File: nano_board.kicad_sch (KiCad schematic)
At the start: 23 parts, among them J1 RJ45

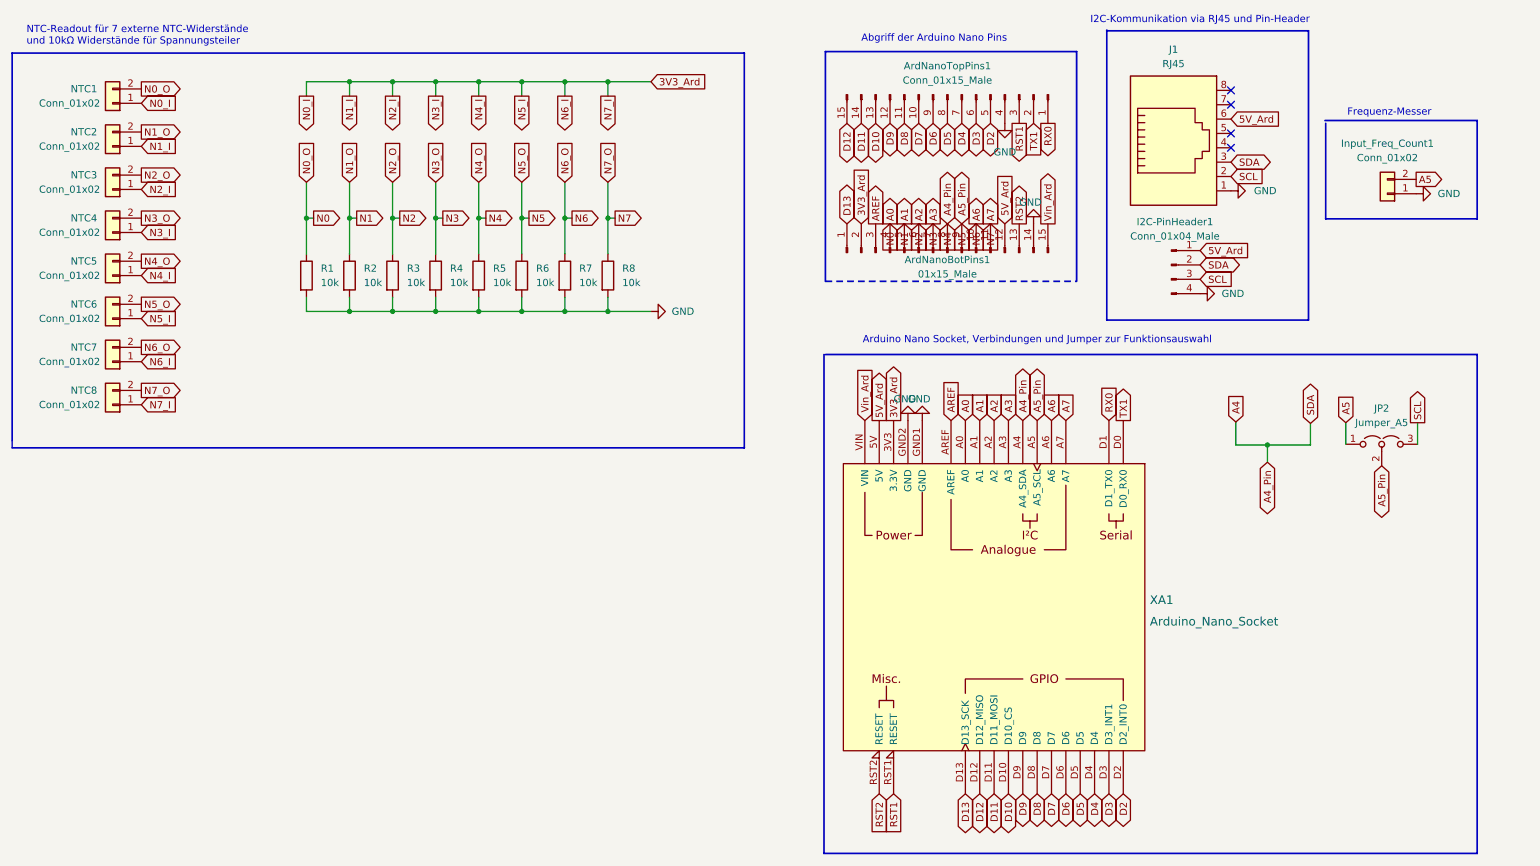
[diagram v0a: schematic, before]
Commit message: ADD: schematic as pdf
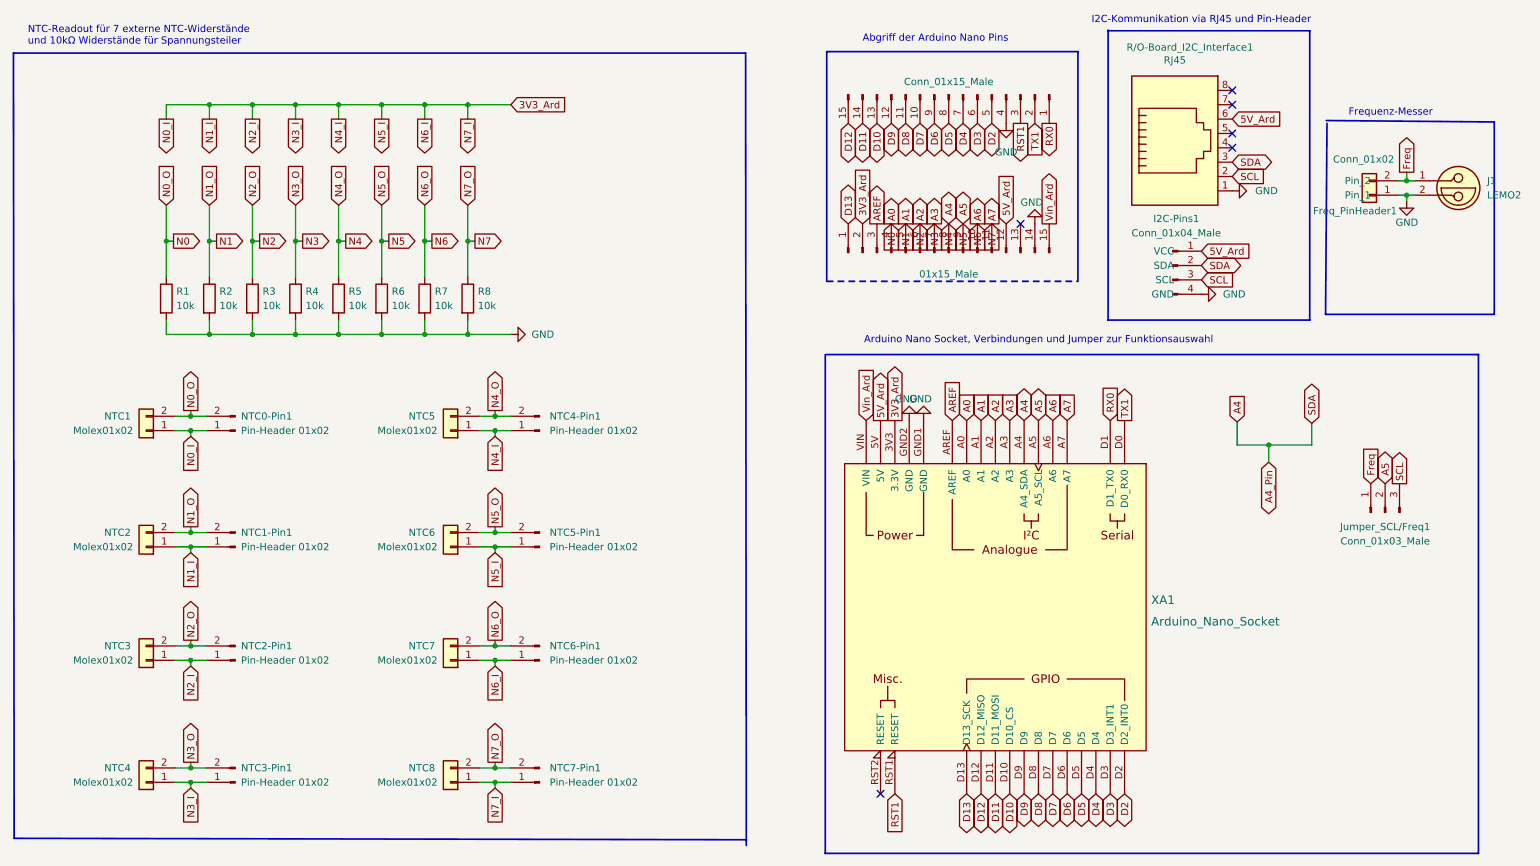
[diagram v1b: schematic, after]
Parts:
- removed JP2: Jumper_A5, Jumper:SolderJumper-3_P1.3mm_Open_Pad1.0x1.5mm_NumberLabels, symbol Jumper:Jumper_3_Open
- added J1: LEMO2, OwnFootprints:EPL.00.250.NTN, symbol Connector:LEMO2
- added Jumper_SCL/Freq1: Conn_01x03_Male, Connector_PinHeader_2.54mm:PinHeader_1x03_P2.54mm_Vertical, symbol Connector:Conn_01x03_Male
- added NTC0-Pin1, NTC1-Pin1, NTC2-Pin1, NTC3-Pin1, NTC4-Pin1, NTC5-Pin1, NTC6-Pin1, NTC7-Pin1: Pin-Header 01x02, Connector_PinHeader_2.54mm:PinHeader_1x02_P2.54mm_Vertical, symbol Connector:Conn_01x02_Male
- NTC1, NTC2, NTC3, NTC4, NTC5, NTC6, NTC7, NTC8: value Conn_01x02 -> Molex01x02
- R/O-Board_I2C_Interface1: renamed from J1; footprint Connector_RJ:RJ45_Plug_Metz_AJP92A8813 -> Connector_RJ:RJ45_Amphenol_RJHSE5380
- renumbered ArdNanoTopPins1 to ArdTopPins1, Input_Freq_Count1 to Freq_PinHeader1, I2C-PinHeader1 to I2C-Pins1
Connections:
- net A5_Pin is gone; now on net A5: ArdNanoBotPins1.9 (Pin_9), NTC6.2 (Pin_2), R6.1, XA1.A5 (A5_SCL)
- net 3V3_Ard: now also NTC0-Pin1.1 (Pin_1), NTC1-Pin1.1 (Pin_1), NTC2-Pin1.1 (Pin_1), NTC3-Pin1.1 (Pin_1), NTC4-Pin1.1 (Pin_1), NTC5-Pin1.1 (Pin_1), NTC6-Pin1.1 (Pin_1), NTC7-Pin1.1 (Pin_1)
- net A0: now also NTC0-Pin1.2 (Pin_2)
- net A1: now also NTC1-Pin1.2 (Pin_2)
- net A2: now also NTC2-Pin1.2 (Pin_2)
- net A3: now also NTC3-Pin1.2 (Pin_2)
- net A4: now also NTC4-Pin1.2 (Pin_2)
- net A5: now also Jumper_SCL/Freq1.2 (Pin_2), NTC5-Pin1.2 (Pin_2); no longer Freq_PinHeader1.2 (Pin_2)
- net A6: now also NTC6-Pin1.2 (Pin_2)
- net A7: now also NTC7-Pin1.2 (Pin_2)
- net GND: now also J1.2
- net SCL: now also Jumper_SCL/Freq1.3 (Pin_3)
- net RST2: no longer names the net of XA1.RST2 (RESET)
- net RST2: no longer ArdNanoBotPins1.13 (Pin_13)
- new net Freq: Freq_PinHeader1.2 (Pin_2), J1.1, Jumper_SCL/Freq1.1 (Pin_1)
- no-connect marks 4 -> 6
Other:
- moved on the sheet: NTC1, R1, R2, R3, R4, R5, R6, R7, R8
